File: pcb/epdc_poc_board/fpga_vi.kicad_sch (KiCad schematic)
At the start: 37 parts, among them J601 DB15_Female_HighDensity_Mount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, J602 Conn_01x15_MountingPin, U201 ECP5U_45_CABGA256, U601 AD9984KCPZ

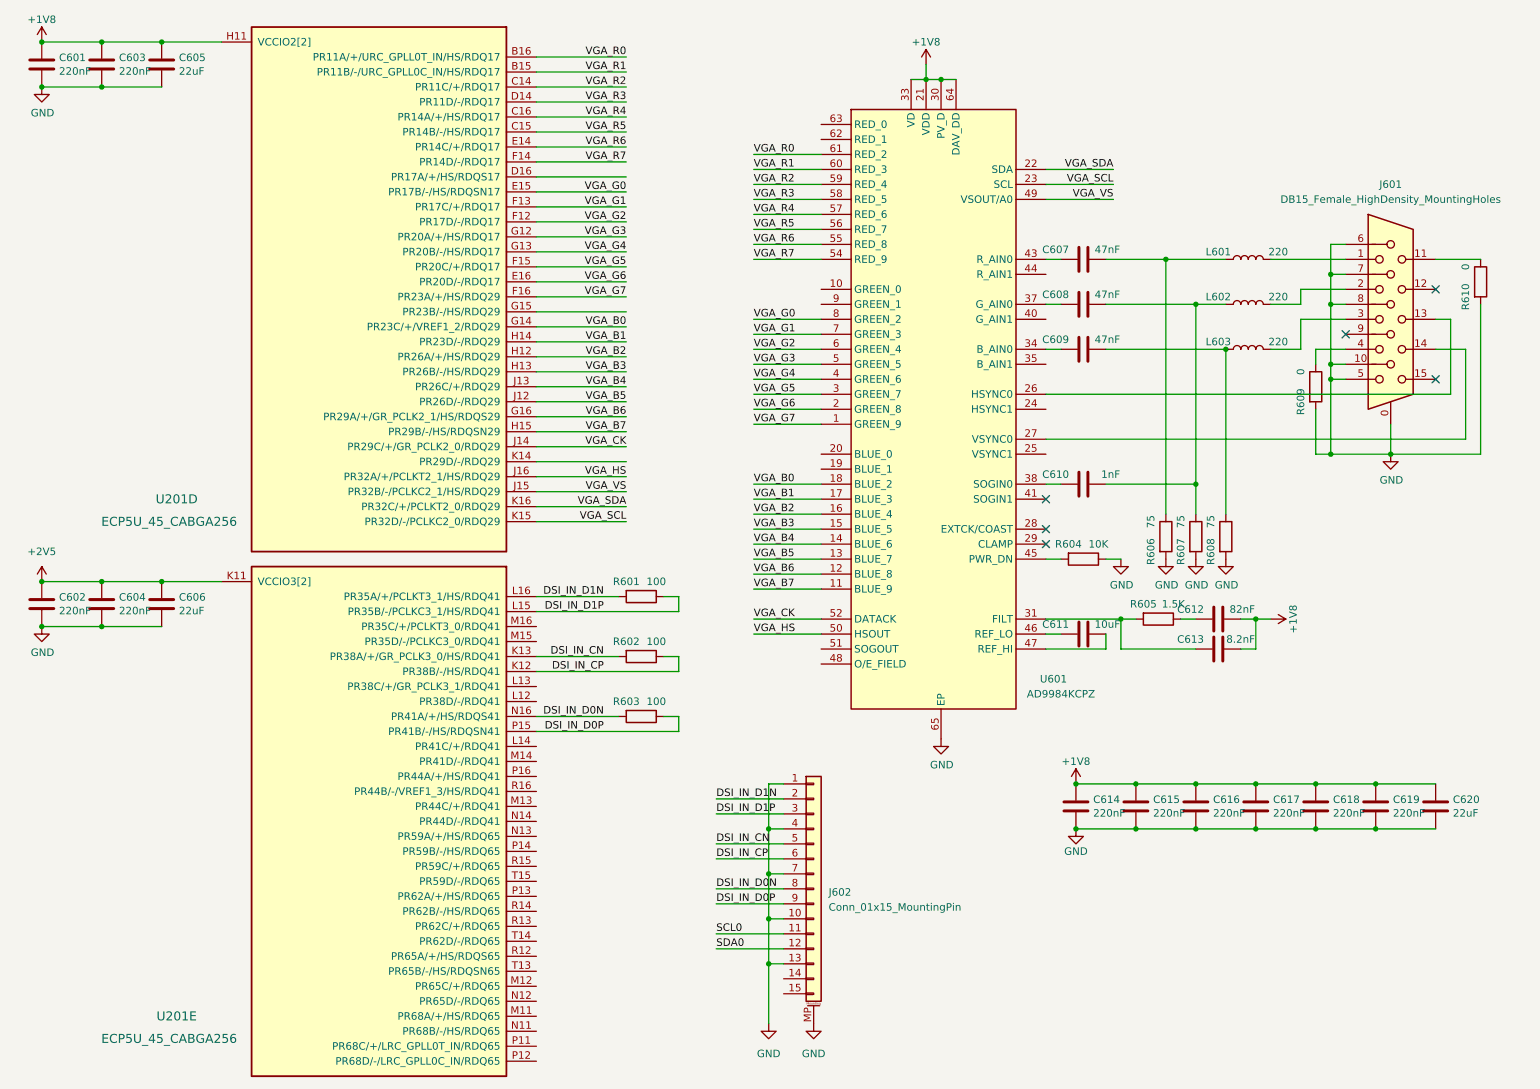
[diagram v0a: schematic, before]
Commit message: - wip epdc poc board, going to remove vga input
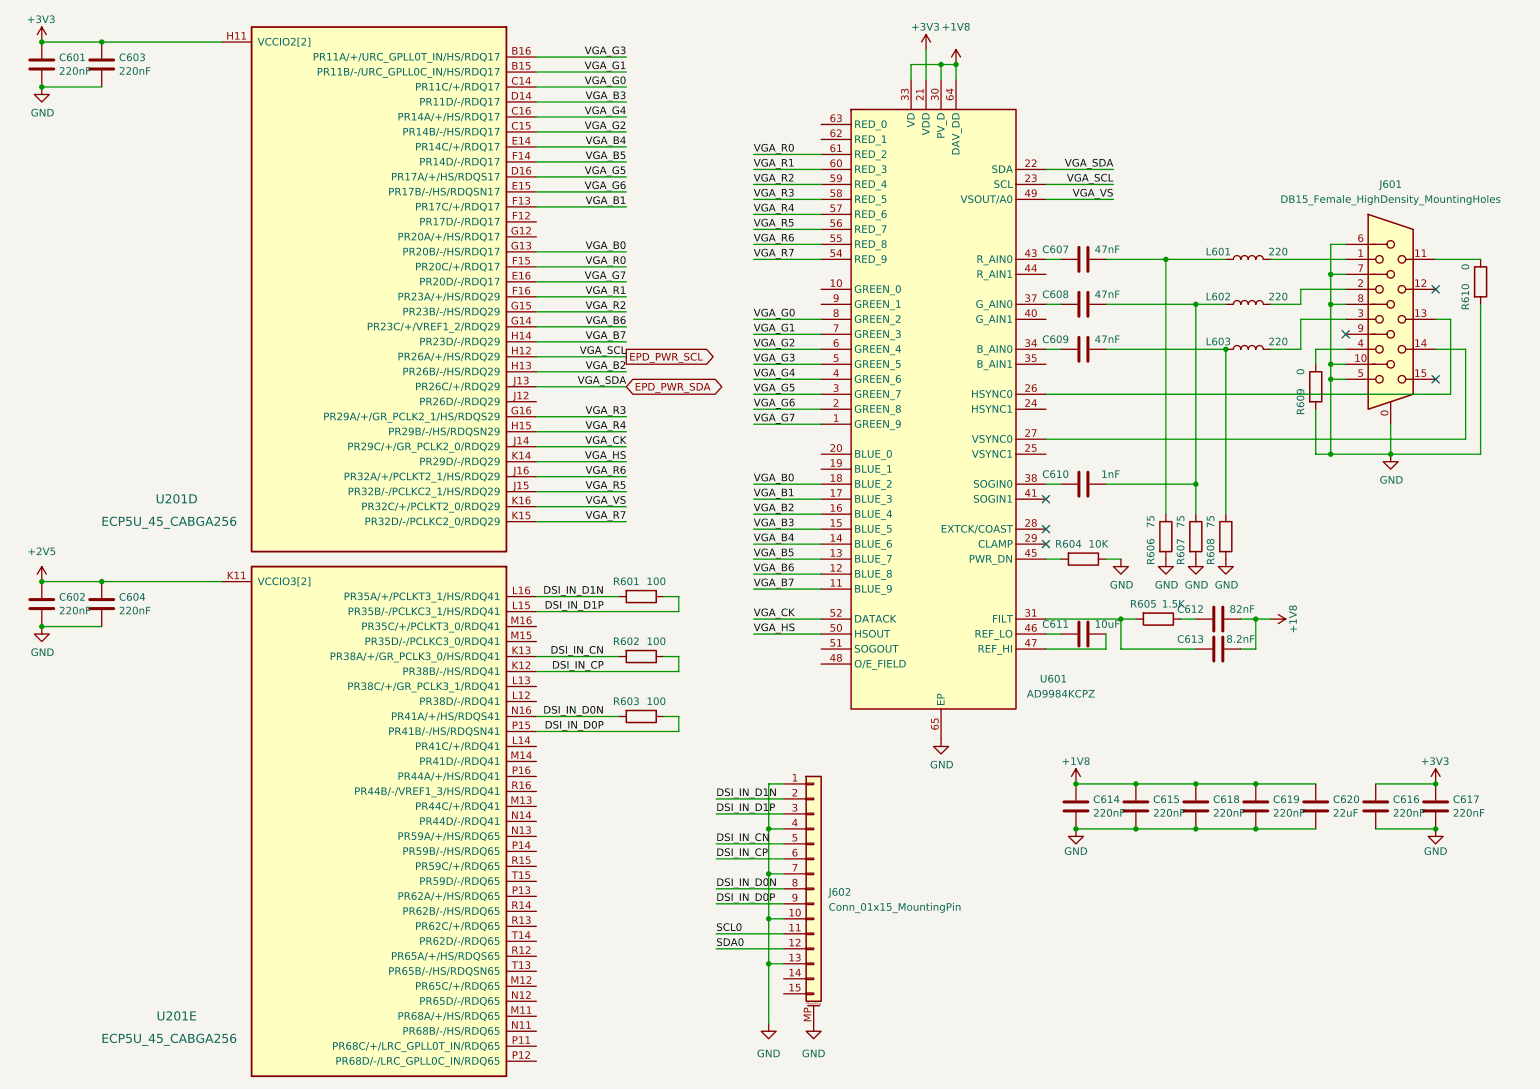
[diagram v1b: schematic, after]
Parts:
- removed C605, C606: 22uF, Capacitor_SMD:C_0603_1608Metric, symbol Device:C
- C612, C613: footprint Capacitor_SMD:C_0603_1608Metric -> Capacitor_SMD:C_0402_1005Metric
- U601: footprint Package_DFN_QFN:QFN-64-1EP_9x9mm_P0.5mm_EP4.7x4.7mm_ThermalVias -> Package_DFN_QFN:QFN-64-1EP_9x9mm_P0.5mm_EP4.7x4.7mm
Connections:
- net +1V8: no longer C601.1, C603.1, C616.1, C617.1, U201.H11 (VCCIO2[2]), U201.J11 (VCCIO2[2]), U601.21 (VDD), U601.53 (VDD)
- net VGA_B0: now also U201.G13 (PR20B/-/HS/RDQ17); no longer U201.G14 (PR23C/+/VREF1_2/RDQ29)
- net VGA_B1: now also U201.F13 (PR17C/+/RDQ17); no longer U201.H14 (PR23D/-/RDQ29)
- net VGA_B2: now also U201.H13 (PR26B/-/HS/RDQ29); no longer U201.H12 (PR26A/+/HS/RDQ29)
- net VGA_B3: now also U201.D14 (PR11D/-/RDQ17); no longer U201.H13 (PR26B/-/HS/RDQ29)
- net VGA_B4: now also U201.E14 (PR14C/+/RDQ17); no longer U201.J13 (PR26C/+/RDQ29)
- net VGA_B5: now also U201.F14 (PR14D/-/RDQ17); no longer U201.J12 (PR26D/-/RDQ29)
- net VGA_B6: now also U201.G14 (PR23C/+/VREF1_2/RDQ29); no longer U201.G16 (PR29A/+/GR_PCLK2_1/HS/RDQS29)
- net VGA_B7: now also U201.H14 (PR23D/-/RDQ29); no longer U201.H15 (PR29B/-/HS/RDQSN29)
- net VGA_G0: now also U201.C14 (PR11C/+/RDQ17); no longer U201.E15 (PR17B/-/HS/RDQSN17)
- net VGA_G1: now also U201.B15 (PR11B/-/URC_GPLL0C_IN/HS/RDQ17); no longer U201.F13 (PR17C/+/RDQ17)
- net VGA_G2: now also U201.C15 (PR14B/-/HS/RDQ17); no longer U201.F12 (PR17D/-/RDQ17)
- net VGA_G3: now also U201.B16 (PR11A/+/URC_GPLL0T_IN/HS/RDQ17); no longer U201.G12 (PR20A/+/HS/RDQ17)
- net VGA_G4: now also U201.C16 (PR14A/+/HS/RDQ17); no longer U201.G13 (PR20B/-/HS/RDQ17)
- net VGA_G5: now also U201.D16 (PR17A/+/HS/RDQS17); no longer U201.F15 (PR20C/+/RDQ17)
- net VGA_G6: now also U201.E15 (PR17B/-/HS/RDQSN17); no longer U201.E16 (PR20D/-/RDQ17)
- net VGA_G7: now also U201.E16 (PR20D/-/RDQ17); no longer U201.F16 (PR23A/+/HS/RDQ29)
- net VGA_HS: now also U201.K14 (PR29D/-/RDQ29); no longer U201.J16 (PR32A/+/PCLKT2_1/HS/RDQ29)
- net VGA_R0: now also U201.F15 (PR20C/+/RDQ17); no longer U201.B16 (PR11A/+/URC_GPLL0T_IN/HS/RDQ17)
- net VGA_R1: now also U201.F16 (PR23A/+/HS/RDQ29); no longer U201.B15 (PR11B/-/URC_GPLL0C_IN/HS/RDQ17)
- net VGA_R2: now also U201.G15 (PR23B/-/HS/RDQ29); no longer U201.C14 (PR11C/+/RDQ17)
- net VGA_R3: now also U201.G16 (PR29A/+/GR_PCLK2_1/HS/RDQS29); no longer U201.D14 (PR11D/-/RDQ17)
- net VGA_R4: now also U201.H15 (PR29B/-/HS/RDQSN29); no longer U201.C16 (PR14A/+/HS/RDQ17)
- net VGA_R5: now also U201.J15 (PR32B/-/PCLKC2_1/HS/RDQ29); no longer U201.C15 (PR14B/-/HS/RDQ17)
- net VGA_R6: now also U201.J16 (PR32A/+/PCLKT2_1/HS/RDQ29); no longer U201.E14 (PR14C/+/RDQ17)
- net VGA_R7: now also U201.K15 (PR32D/-/PCLKC2_0/RDQ29); no longer U201.F14 (PR14D/-/RDQ17)
- net VGA_VS: now also U201.K16 (PR32C/+/PCLKT2_0/RDQ29); no longer U201.J15 (PR32B/-/PCLKC2_1/HS/RDQ29)
- net VGA_SCL renamed EPD_PWR_SCL
- net EPD_PWR_SCL: now also U201.H12 (PR26A/+/HS/RDQ29); no longer U201.K15 (PR32D/-/PCLKC2_0/RDQ29)
- net VGA_SDA renamed EPD_PWR_SDA
- net EPD_PWR_SDA: now also U201.J13 (PR26C/+/RDQ29); no longer U201.K16 (PR32C/+/PCLKT2_0/RDQ29)
- new net +3V3: C601.1, C603.1, C616.1, C617.1, U201.H11 (VCCIO2[2]), U201.J11 (VCCIO2[2]), U601.21 (VDD), U601.53 (VDD)
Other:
- moved on the sheet: C616, C617, C618, C619, C620

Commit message: pcb: switch to s6 for epdc board
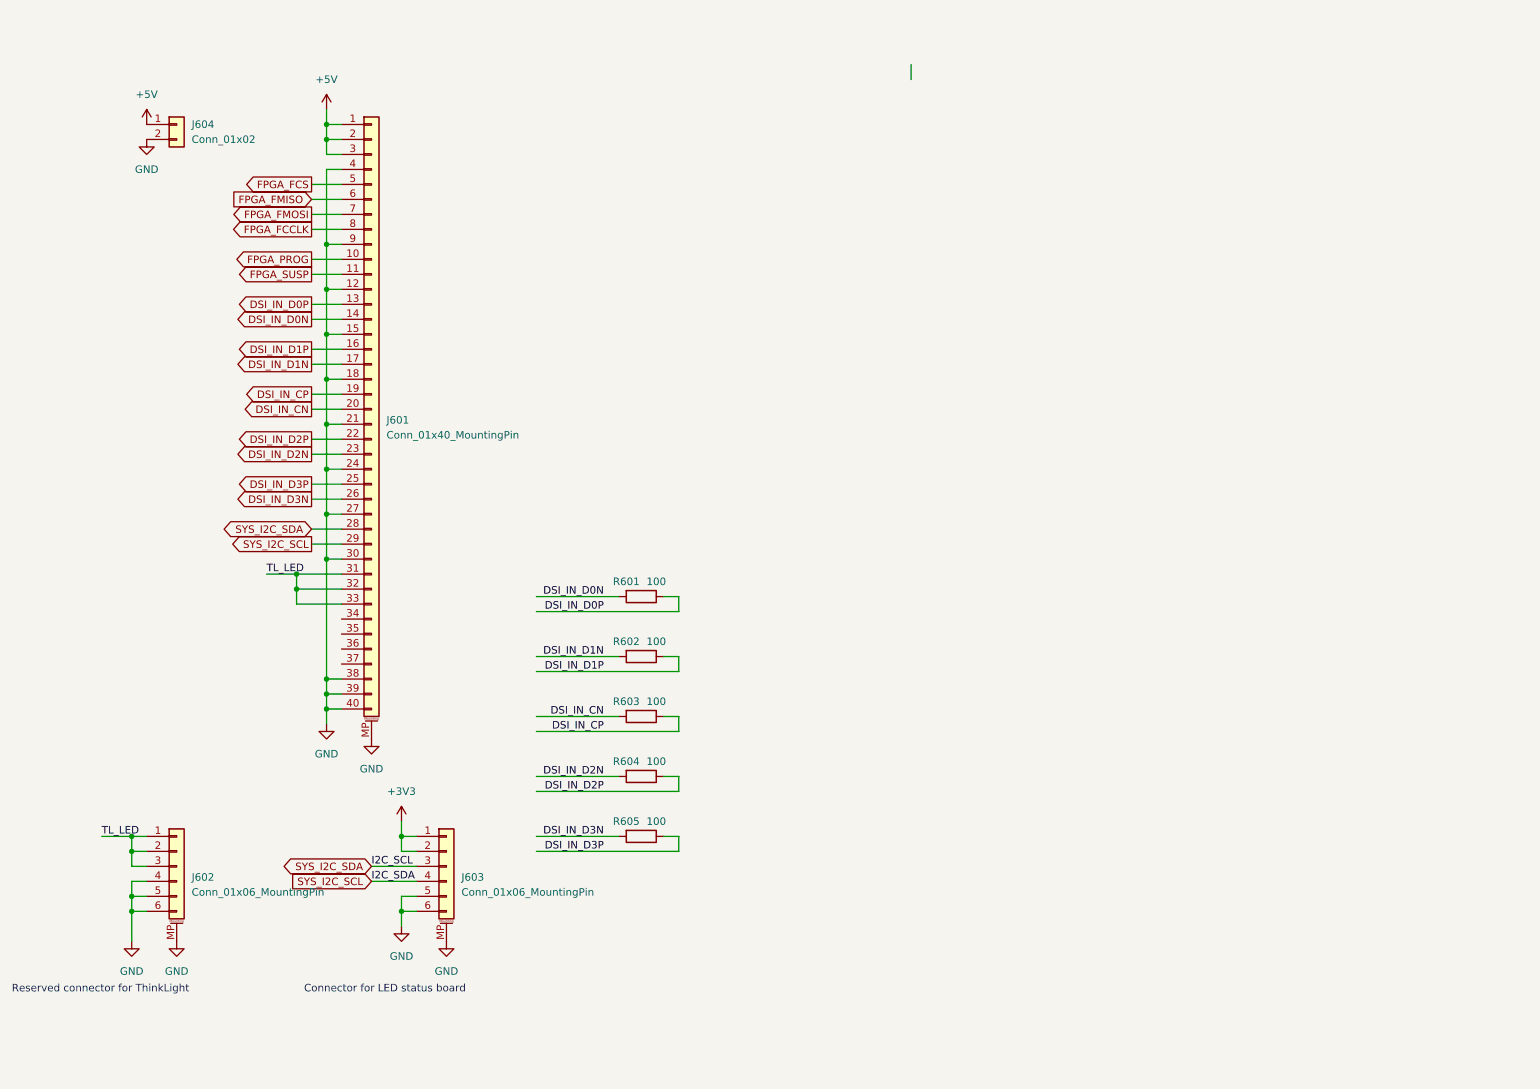
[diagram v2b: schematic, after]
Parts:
- removed C601, C602, C603, C604, C614, C615, C616, C617, C618, C619: 220nF, Capacitor_SMD:C_0402_1005Metric, symbol Device:C
- removed C607, C608, C609: 47nF, Capacitor_SMD:C_0402_1005Metric, symbol Device:C
- removed C610: 1nF, Capacitor_SMD:C_0402_1005Metric, symbol Device:C
- removed C611: 10uF, Capacitor_SMD:C_0603_1608Metric, symbol Device:C
- removed C612: 82nF, Capacitor_SMD:C_0402_1005Metric, symbol Device:C
- removed C613: 8.2nF, Capacitor_SMD:C_0402_1005Metric, symbol Device:C
- removed C620: 22uF, Capacitor_SMD:C_0603_1608Metric, symbol Device:C
- removed J601: DB15_Female_HighDensity_MountingHoles, Connector_Dsub:DSUB-15-HD_Female_Horizontal_P2.29x1.98mm_EdgePinOffset3.03mm_Housed_MountingHolesOffset4.94mm, symbol Connector:DB15_Female_HighDensity_MountingHoles
- removed J602: Conn_01x15_MountingPin, Connector_FFC-FPC:TE_1-84952-5_1x15-1MP_P1.0mm_Horizontal, symbol Connector_Generic_MountingPin:Conn_01x15_MountingPin
- removed L601, L602, L603: 220, Inductor_SMD:L_0402_1005Metric, symbol Device:L
- removed R606, R607, R608: 75, Resistor_SMD:R_0402_1005Metric, symbol Device:R
- removed R609, R610: 0, Resistor_SMD:R_0402_1005Metric, symbol Device:R
- removed U201: ECP5U_45_CABGA256, Package_BGA:BGA-256_14.0x14.0mm_Layout16x16_P0.8mm_Ball0.45mm_Pad0.32mm_NSMD, symbol symbols:ECP5U_45_CABGA256
- removed U601: AD9984KCPZ, Package_DFN_QFN:QFN-64-1EP_9x9mm_P0.5mm_EP4.7x4.7mm, symbol symbols:AD9984KCPZ
- added J601: Conn_01x40_MountingPin, Connector_FFC-FPC:Hirose_FH12-40S-0.5SH_1x40-1MP_P0.50mm_Horizontal, symbol Connector_Generic_MountingPin:Conn_01x40_MountingPin
- added J602, J603: Conn_01x06_MountingPin, Connector_FFC-FPC:Hirose_FH12-6S-0.5SH_1x06-1MP_P0.50mm_Horizontal, symbol Connector_Generic_MountingPin:Conn_01x06_MountingPin
- added J604: Conn_01x02, Connector_PinHeader_2.54mm:PinHeader_1x02_P2.54mm_Vertical, symbol Connector_Generic:Conn_01x02
- R604: value 10K -> 100
- R605: value 1.5K -> 100
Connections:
- net +3V3: now also J603.1 (Pin_1), J603.2 (Pin_2)
- net DSI_IN_CN: now also R603.2, J601.20 (Pin_20); no longer R602.2
- net DSI_IN_CP: now also R603.1, J601.19 (Pin_19); no longer R602.1
- net DSI_IN_D0N: now also R601.2, J601.14 (Pin_14); no longer R603.2
- net DSI_IN_D0P: now also R601.1, J601.13 (Pin_13); no longer R603.1
- net DSI_IN_D1N: now also R602.2, J601.17 (Pin_17); no longer R601.2
- net DSI_IN_D1P: now also R602.1, J601.16 (Pin_16); no longer R601.1
- net GND: now also J601.12 (Pin_12), J601.15 (Pin_15), J601.18 (Pin_18), J601.21 (Pin_21), J601.24 (Pin_24), J601.27 (Pin_27), J601.30 (Pin_30), J601.38 (Pin_38), J601.39 (Pin_39), J601.4 (Pin_4), J601.40 (Pin_40), J601.9 (Pin_9), J601.MP (MountPin), J602.4 (Pin_4), J602.5 (Pin_5), J602.6 (Pin_6), J602.MP (MountPin), J603.5 (Pin_5), J603.6 (Pin_6), J603.MP (MountPin), J604.2 (Pin_2); no longer R604.1
- net DSI_IN_D3P: now reaches R605.1
- net DSI_IN_D3P: now also J601.25 (Pin_25)
- net DSI_IN_D3N: now reaches R605.2
- net DSI_IN_D3N: now also J601.26 (Pin_26)
- net DSI_IN_D2N: now reaches R604.2
- net DSI_IN_D2N: now also J601.23 (Pin_23)
- new net +5V: J601.1 (Pin_1), J601.2 (Pin_2), J601.3 (Pin_3), J604.1 (Pin_1)
- new net DSI_IN_D2P: J601.22 (Pin_22), R604.1
- new net FPGA_FCCLK: J601.8 (Pin_8)
- new net FPGA_FCS: J601.5 (Pin_5)
- new net FPGA_FMISO: J601.6 (Pin_6)
- new net FPGA_FMOSI: J601.7 (Pin_7)
- new net FPGA_PROG: J601.10 (Pin_10)
- new net FPGA_SUSP: J601.11 (Pin_11)
- new net SYS_I2C_SCL: J601.29 (Pin_29), J603.4 (Pin_4)
- new net SYS_I2C_SDA: J601.28 (Pin_28), J603.3 (Pin_3)
- new net TL_LED: J601.31 (Pin_31), J601.32 (Pin_32), J601.33 (Pin_33), J602.1 (Pin_1), J602.2 (Pin_2), J602.3 (Pin_3)
- no-connect marks 6 -> 0
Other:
- note added: "Connector for LED status board"
- note added: "Reserved connector for ThinkLight"
